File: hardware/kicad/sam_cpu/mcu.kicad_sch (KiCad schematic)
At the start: 50 parts, among them J19 USB-C (to Pi), J20 SWD, J21 Raspberry Pi 40-pin, SW1 RESET, SW2 BOOTSEL, U25 DS3231MZ, U4 RP2354B, U5 TPS3808G33, Y1 12MHz

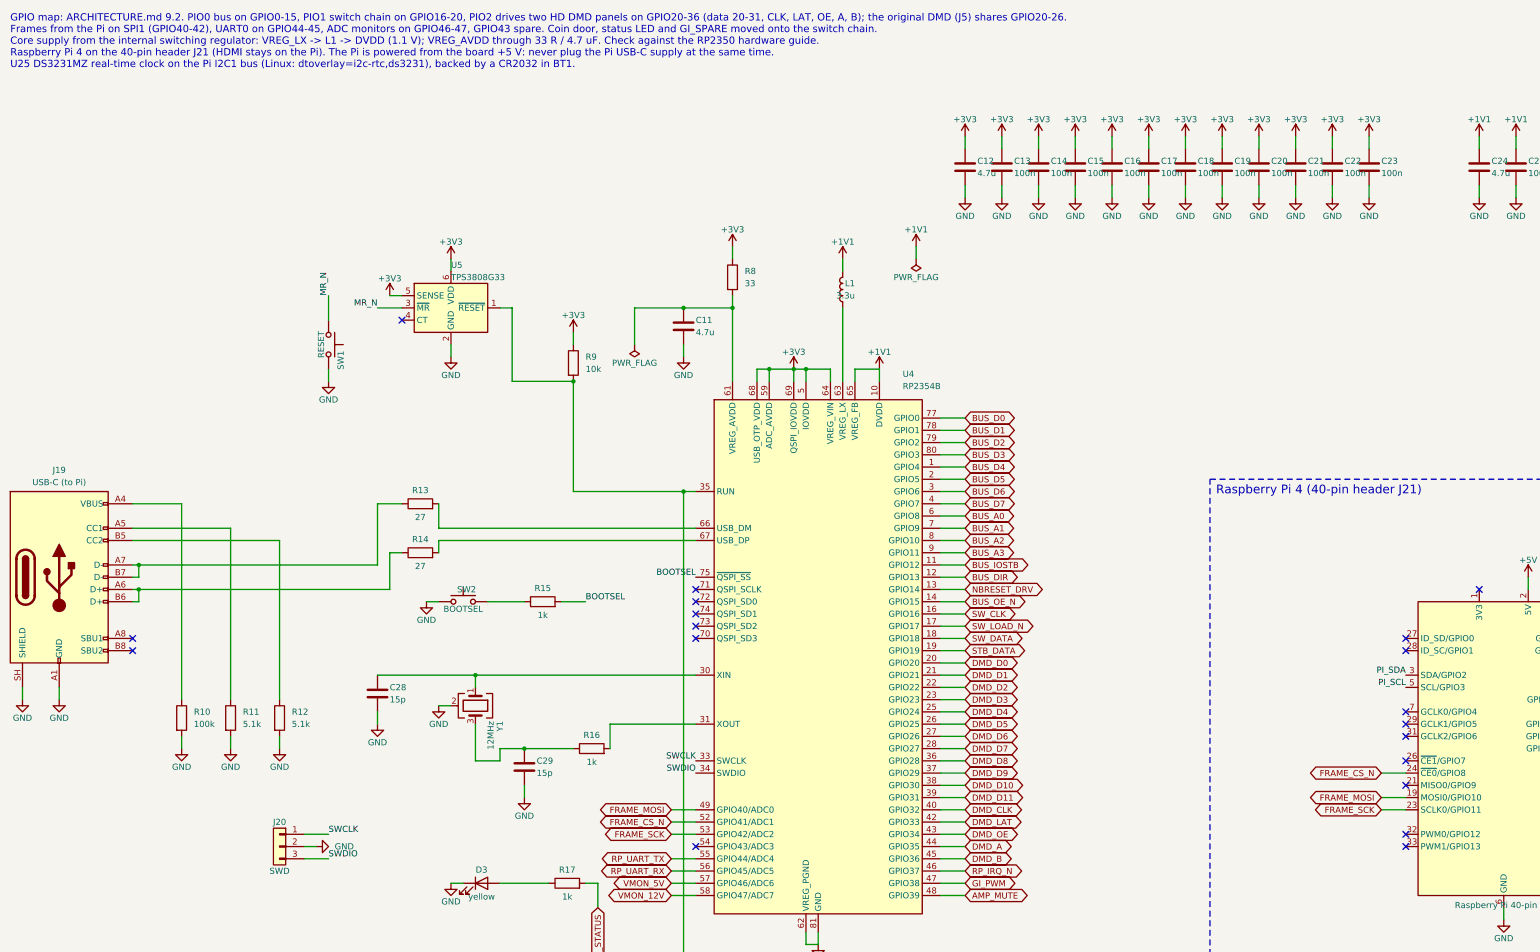
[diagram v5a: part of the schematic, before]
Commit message: Remove both DMD interfaces from the schematic and the board
DMD signals do not survive the long cabinet wires (Vincent, 2026-10-07).
Removed: J5 original DMD driver (U21, RN4, RN5, R176-R182, C95) and the
HD panel bus (J25, J26, U27-U29, RN6-RN11, C122-C124, TP23, TP24), their
tracks and fan-out vias. U30 / U31 stay (switch chain). RP2354B GPIO20-36
are unassigned (no-connect flags). The board goes back to the original
120.65 x 231.76 mm outline. DRC: 20 connections still open (was 35).

Co-Authored-By: Claude Opus 5.5 (1M context) <noreply@anthropic.com>
Claude-Session: https://claude.ai/code/session_01ExuDVoDDDHhVWjb8EwVzYb
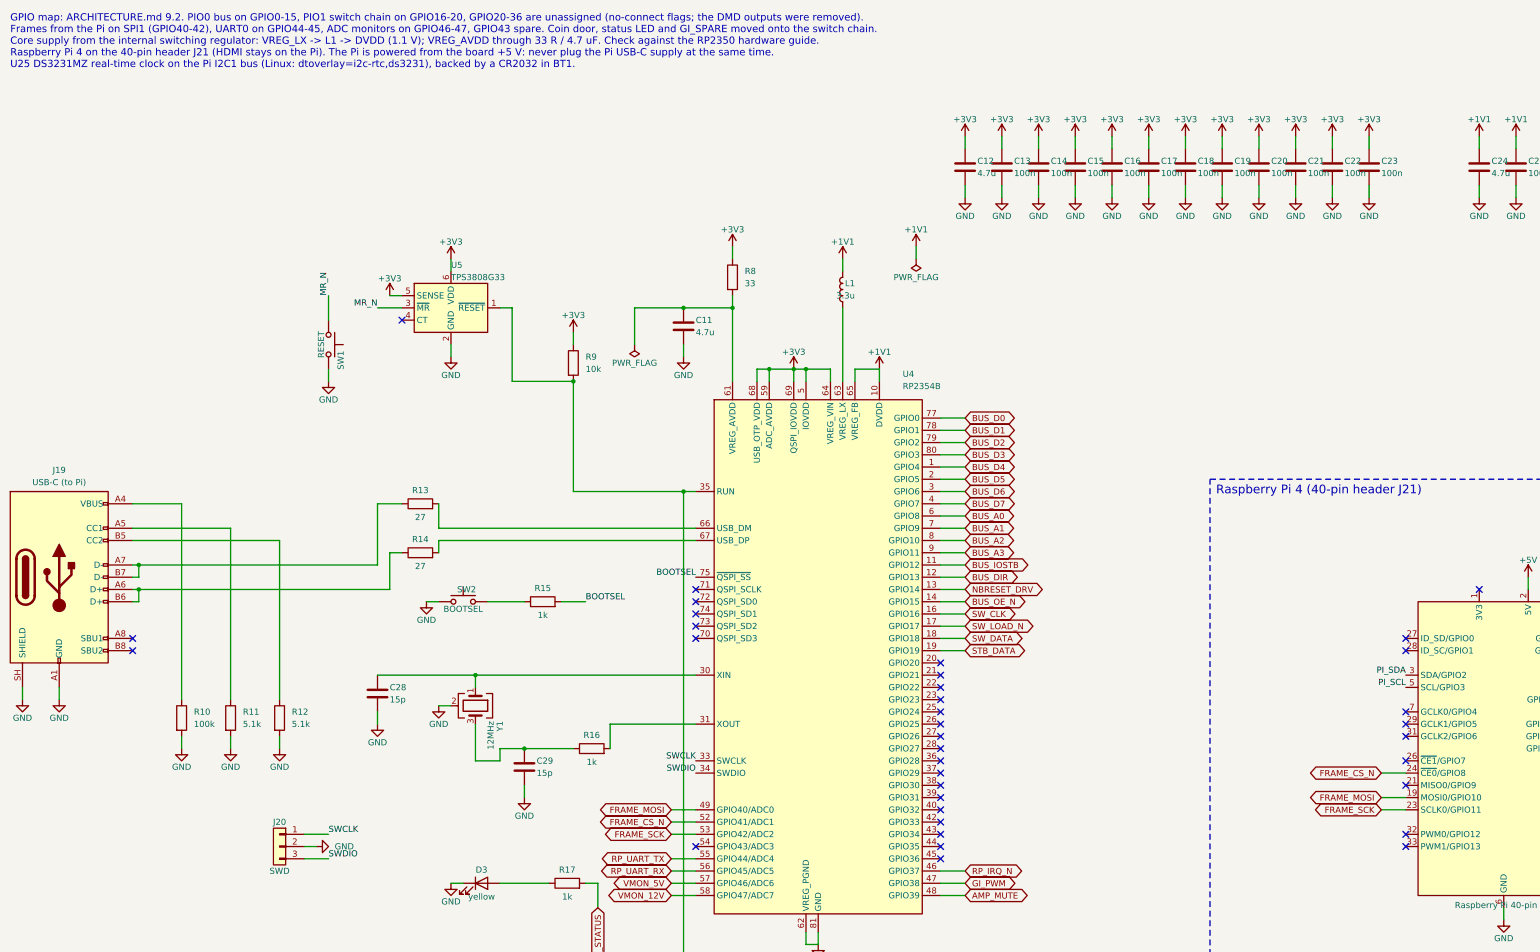
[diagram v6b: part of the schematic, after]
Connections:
- net DMD_A: no longer names the net of U4.44 (GPIO35)
- net DMD_B: no longer names the net of U4.45 (GPIO36)
- net DMD_CLK: no longer names the net of U4.40 (GPIO32)
- net DMD_D0: no longer names the net of U4.20 (GPIO20)
- net DMD_D1: no longer names the net of U4.21 (GPIO21)
- net DMD_D10: no longer names the net of U4.38 (GPIO30)
- net DMD_D11: no longer names the net of U4.39 (GPIO31)
- net DMD_D2: no longer names the net of U4.22 (GPIO22)
- net DMD_D3: no longer names the net of U4.23 (GPIO23)
- net DMD_D4: no longer names the net of U4.25 (GPIO24)
- net DMD_D5: no longer names the net of U4.26 (GPIO25)
- net DMD_D6: no longer names the net of U4.27 (GPIO26)
- net DMD_D7: no longer names the net of U4.28 (GPIO27)
- net DMD_D8: no longer names the net of U4.36 (GPIO28)
- net DMD_D9: no longer names the net of U4.37 (GPIO29)
- net DMD_LAT: no longer names the net of U4.42 (GPIO33)
- net DMD_OE: no longer names the net of U4.43 (GPIO34)
- no-connect marks 26 -> 43
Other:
- note added: "GPIO map: ARCHITECTURE.md 9.2. PIO0 bus on GPIO0-15, PIO1 switch chain on GPIO16-20, GPIO20-36 are unassigned (no-connect flags; the DMD outputs were removed). Frames from the Pi on SPI1 (GPIO40-42), UART0 on GPIO44-45, ADC monitors on GPIO46-47, GPIO43 spare. Coin door, status LED and GI_SPARE moved onto the switch chain. Core supply from the internal switching regulator: VREG_LX -> L1 -> DVDD (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"
- note removed: "GPIO map: ARCHITECTURE.md 9.2. PIO0 bus on GPIO0-15, PIO1 switch chain on GPIO16-20, PIO2 drives two HD DMD panels on GPIO20-36 (data 20-31, CLK, LAT, OE, A, B); the original DMD (J5) shares GPIO20-26. Frames from the Pi on SPI1 (GPIO40-42), UART0 on GPIO44-45, ADC monitors on GPIO46-47, GPIO43 spare. Coin door, status LED and GI_SPARE moved onto the switch chain. Core supply from the internal sw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"

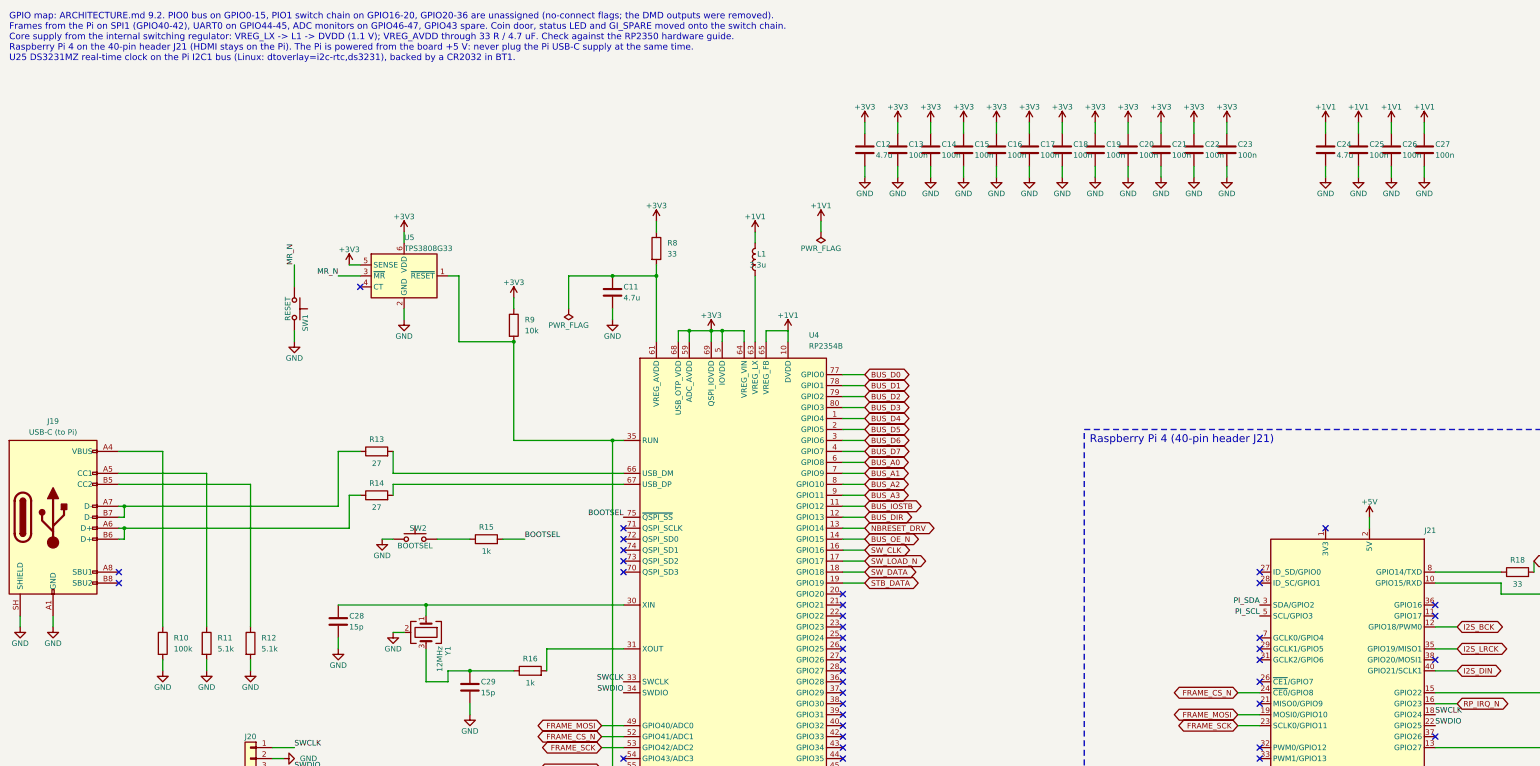
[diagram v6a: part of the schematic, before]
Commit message: Add an RS485 port (RJ45) and an I2S input header
Vincent, 2026-10-07: one RS485 port for both set-ups. With the Pi on J21
it is the Pi's UART3 (GPIO4 / 5, RTS on GPIO7 as driver enable); with a
remote Pi it is the RP2354B's UART1 (GPIO20 / 21, GPIO22 driver enable),
and the remote Pi's I2S reaches the DAC on J28. Both sides reach the
THVD1450 through 1 k, so only the configured side drives.

New page 13 (U32, R204-R212, C127, D27, JP2, J27, J28), RS485 labels on
the MCU sheet, and the 15 footprints placed without moving any part: the
RJ45 on the right edge where J5 was. README / PCB.md updated for draft 0.6
(DMD removal included). ERC clean; the new nets are not routed yet.

Co-Authored-By: Claude Opus 5.5 (1M context) <noreply@anthropic.com>
Claude-Session: https://claude.ai/code/session_01ExuDVoDDDHhVWjb8EwVzYb
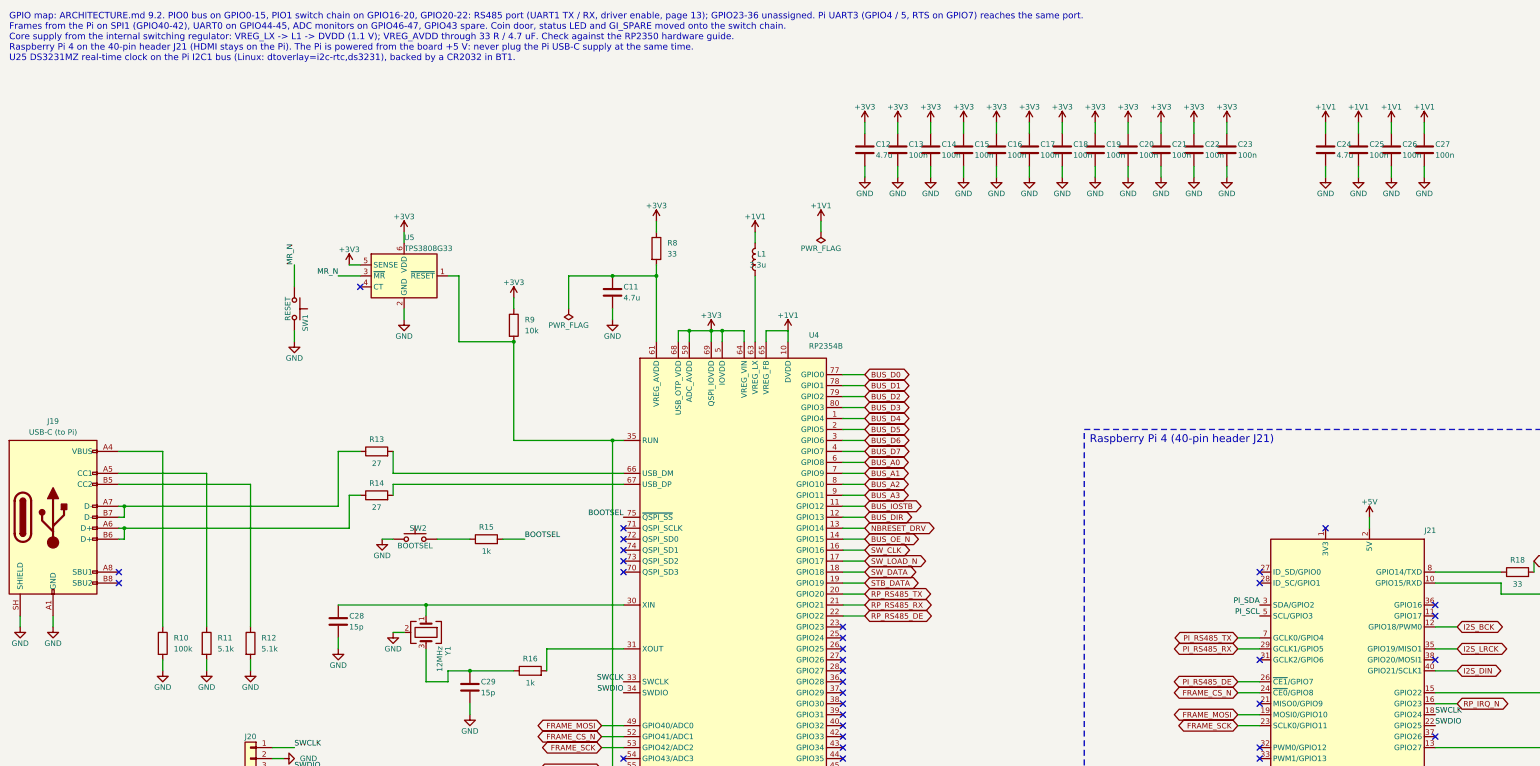
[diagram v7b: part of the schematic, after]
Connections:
- net PI_RS485_DE: now reaches J21.26 (~{CE1}/GPIO7)
- net PI_RS485_RX: now reaches J21.29 (GCLK1/GPIO5)
- net PI_RS485_TX: now reaches J21.7 (GCLK0/GPIO4)
- net RP_RS485_TX: now reaches U4.20 (GPIO20)
- net RP_RS485_RX: now reaches U4.21 (GPIO21)
- net RP_RS485_DE: now reaches U4.22 (GPIO22)
- no-connect marks 43 -> 37
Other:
- note added: "GPIO map: ARCHITECTURE.md 9.2. PIO0 bus on GPIO0-15, PIO1 switch chain on GPIO16-20, GPIO20-22: RS485 port (UART1 TX / RX, driver enable, page 13); GPIO23-36 unassigned. Pi UART3 (GPIO4 / 5, RTS on GPIO7) reaches the same port. Frames from the Pi on SPI1 (GPIO40-42), UART0 on GPIO44-45, ADC monitors on GPIO46-47, GPIO43 spare. Coin door, status LED and GI_SPARE moved onto the switch chain. Core s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"
- note removed: "GPIO map: ARCHITECTURE.md 9.2. PIO0 bus on GPIO0-15, PIO1 switch chain on GPIO16-20, GPIO20-36 are unassigned (no-connect flags; the DMD outputs were removed). Frames from the Pi on SPI1 (GPIO40-42), UART0 on GPIO44-45, ADC monitors on GPIO46-47, GPIO43 spare. Coin door, status LED and GI_SPARE moved onto the switch chain. Core supply from the internal switching regulator: VREG_LX -> L1 -> DVDD (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"
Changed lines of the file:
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@@
 		)
 	)
-	(text "GPIO map: ARCHITECTURE.md 9.2. PIO0 bus on GPIO0-15, PIO1 switch chain on GPIO16-20, GPIO20-36 are unassigned (no-connect flags; the DMD outputs were removed).\nFrames from the Pi on SPI1 (GPIO40-42), UART0 on GPIO44-45, ADC monitors on GPIO46-47, GPIO43 spare. Coin door, status LED and GI_SPARE moved onto the switch chain.\nCore supply from the internal switching regulator: VREG_LX -> L1 -> DVDD (1.1 V); VREG_AVDD through 33 R / 4.7 uF. Check against the RP2350 hardware guide.\nRaspberry Pi 4 on the 40-pin header J21 (HDMI stays on the Pi). The Pi is powered from the board +5 V: never plug the Pi USB-C supply at the same time.\nU25 DS3231MZ real-time clock on the Pi I2C1 bus (Linux: dtoverlay=i2c-rtc,ds3231), backed by a CR2032 in BT1."
+	(text "GPIO map: ARCHITECTURE.md 9.2. PIO0 bus on GPIO0-15, PIO1 switch chain on GPIO16-20, GPIO20-22: RS485 port (UART1 TX / RX, driver enable, page 13); GPIO23-36 unassigned. Pi UART3 (GPIO4 / 5, RTS on GPIO7) reaches the same port.\nFrames from the Pi on SPI1 (GPIO40-42), UART0 on GPIO44-45, ADC monitors on GPIO46-47, GPIO43 spare. Coin door, status LED and GI_SPARE moved onto the switch chain.\nCore supply from the internal switching regulator: VREG_LX -> L1 -> DVDD (1.1 V); VREG_AVDD through 33 R / 4.7 uF. Check against the RP2350 hardware guide.\nRaspberry Pi 4 on the 40-pin header J21 (HDMI stays on the Pi). The Pi is powered from the board +5 V: never plug the Pi USB-C supply at the same time.\nU25 DS3231MZ real-time clock on the Pi I2C1 bus (Linux: dtoverlay=i2c-rtc,ds3231), backed by a CR2032 in BT1."
 		(exclude_from_sim no)
 		(at 15.24 15.24 0)
@@
 	)
 	(no_connect
-		(at 304.8 162.56)
-	)
-	(no_connect
 		(at 304.8 165.1)
 	)
@@
 	)
 	(no_connect
-		(at 304.8 160.02)
-	)
-	(no_connect
-		(at 304.8 170.18)
-	)
-	(no_connect
 		(at 73.66 259.08)
 	)
@@
 	)
 	(no_connect
-		(at 208.28 149.86)
-	)
-	(no_connect
-		(at 208.28 154.94)
-	)
-	(no_connect
 		(at 208.28 190.5)
 	)
@@
 	)
 	(no_connect
-		(at 208.28 152.4)
-	)
-	(no_connect
 		(at 208.28 170.18)
 	)
@@
 		(at 208.28 185.42)
 	)
+	(wire
+		(pts
+			(xy 304.8 160.02) (xy 299.72 160.02)
+		)
+		(stroke
+			(width 0)
+			(type default)
+		)
+	)
+	(global_label "PI_RS485_TX"
+		(shape bidirectional)
+		(at 299.72 160.02 180)
+		(fields_autoplaced yes)
+		(effects
+			(font
+				(size 1.27 1.27)
+			)
+			(justify right)
+		)
+		(property "Intersheetrefs" "${INTERSHEET_REFS}"
+			(at 282.67 160.02 180)
+			(show_name no)
+			(do_not_autoplace no)
+			(effects
+				(font
+					(size 1.27 1.27)
+				)
+				(justify right)
+			)
+		)
+	)
+	(wire
+		(pts
+			(xy 304.8 162.56) (xy 299.72 162.56)
+		)
+		(stroke
+			(width 0)
+			(type default)
+		)
+	)
+	(global_label "PI_RS485_RX"
+		(shape bidirectional)
+		(at 299.72 162.56 180)
+		(fields_autoplaced yes)
+		(effects
+			(font
+				(size 1.27 1.27)
+			)
+			(justify right)
+		)
+		(property "Intersheetrefs" "${INTERSHEET_REFS}"
+			(at 282.67 162.56 180)
+			(show_name no)
+			(do_not_autoplace no)
+			(effects
+				(font
+					(size 1.27 1.27)
+				)
+				(justify right)
+			)
+		)
+	)
+	(wire
+		(pts
+			(xy 304.8 170.18) (xy 299.72 170.18)
+		)
+		(stroke
+			(width 0)
+			(type default)
+		)
+	)
+	(global_label "PI_RS485_DE"
+		(shape bidirectional)
+		(at 299.72 170.18 180)
+		(fields_autoplaced yes)
+		(effects
+			(font
+				(size 1.27 1.27)
+			)
+			(justify right)
+		)
+		(property "Intersheetrefs" "${INTERSHEET_REFS}"
+			(at 282.67 170.18 180)
+			(show_name no)
+			(do_not_autoplace no)
+			(effects
+				(font
+					(size 1.27 1.27)
+				)
+				(justify right)
+			)
+		)
+	)
+	(wire
+		(pts
+			(xy 208.28 149.86) (xy 213.36 149.86)
+		)
+		(stroke
+			(width 0)
+			(type default)
+		)
+	)
+	(global_label "RP_RS485_TX"
+		(shape bidirectional)
+		(at 213.36 149.86 0)
+		(fields_autoplaced yes)
+		(effects
+			(font
+				(size 1.27 1.27)
+			)
+			(justify left)
+		)
+		(property "Intersheetrefs" "${INTERSHEET_REFS}"
+			(at 230.41 149.86 0)
+			(show_name no)
+			(do_not_autoplace no)
+			(effects
+				(font
+					(size 1.27 1.27)
+				)
+				(justify left)
+			)
+		)
+	)
+	(wire
+		(pts
+			(xy 208.28 154.94) (xy 213.36 154.94)
+		)
+		(stroke
+			(width 0)
+			(type default)
+		)
+	)
+	(global_label "RP_RS485_DE"
+		(shape bidirectional)
+		(at 213.36 154.94 0)
+		(fields_autoplaced yes)
+		(effects
+			(font
+				(size 1.27 1.27)
+			)
+			(justify left)
+		)
+		(property "Intersheetrefs" "${INTERSHEET_REFS}"
+			(at 230.41 154.94 0)
+			(show_name no)
+			(do_not_autoplace no)
+			(effects
+				(font
+					(size 1.27 1.27)
+				)
+				(justify left)
+			)
+		)
+	)
+	(wire
+		(pts
+			(xy 208.28 152.4) (xy 213.36 152.4)
+		)
+		(stroke
+			(width 0)
+			(type default)
+		)
+	)
+	(global_label "RP_RS485_RX"
+		(shape bidirectional)
+		(at 213.36 152.4 0)
+		(fields_autoplaced yes)
+		(effects
+			(font
+				(size 1.27 1.27)
+			)
+			(justify left)
+		)
+		(property "Intersheetrefs" "${INTERSHEET_REFS}"
+			(at 230.41 152.4 0)
+			(show_name no)
+			(do_not_autoplace no)
+			(effects
+				(font
+					(size 1.27 1.27)
+				)
+				(justify left)
+			)
+		)
+	)
 )
